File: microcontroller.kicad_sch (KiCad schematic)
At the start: 0 parts

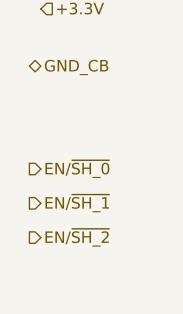
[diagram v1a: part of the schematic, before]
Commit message: Removed hierarchical labels on the sensor board (4 slot) in favour of local labels and connectors. The idea was that the sensor boards are plug-ins so having them defined as separate boards makes more sense. Eventually I think we'll pull them out of the main schematic and design each one separately with the common connector pinout.
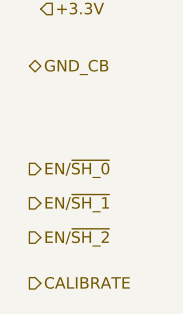
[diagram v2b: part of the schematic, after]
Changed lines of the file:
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@@
+		)
+	)
+	(hierarchical_label "CALIBRATE"
+		(shape output)
+		(at 241.3 142.24 0)
+		(effects
+			(font
+				(size 1.27 1.27)
+			)
+			(justify left)
 		)
 	)

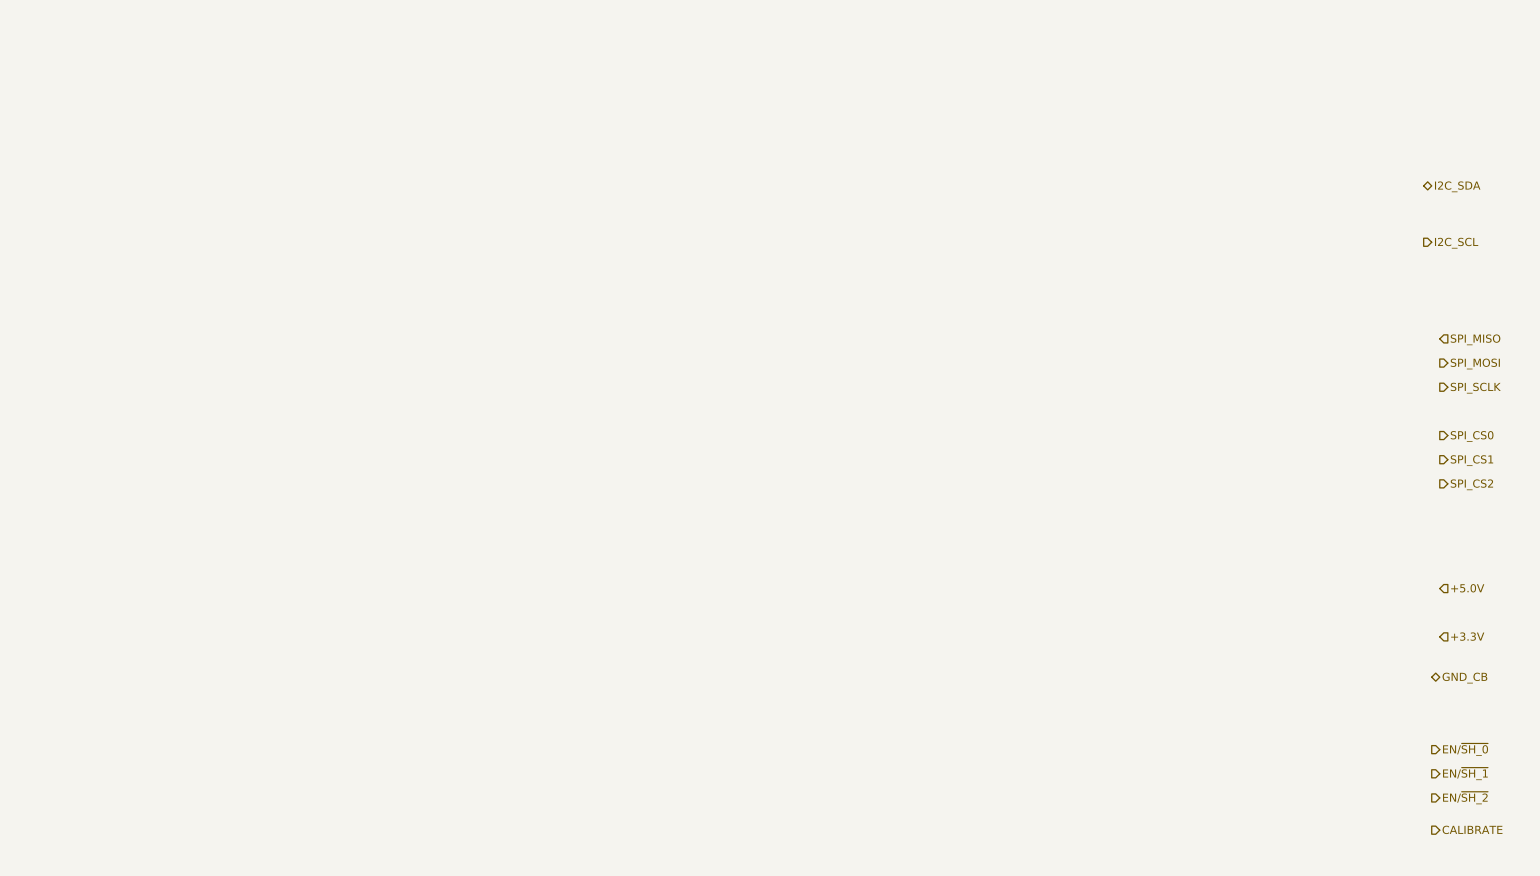
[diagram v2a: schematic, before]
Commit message: Added some notes to otherwise blank pages. Added the full 8 sensor buffers to the 8 sensor analog board. Added a decoupling sub page to same. Changed a couple of sensor labels on base and 4 board just as placeholders
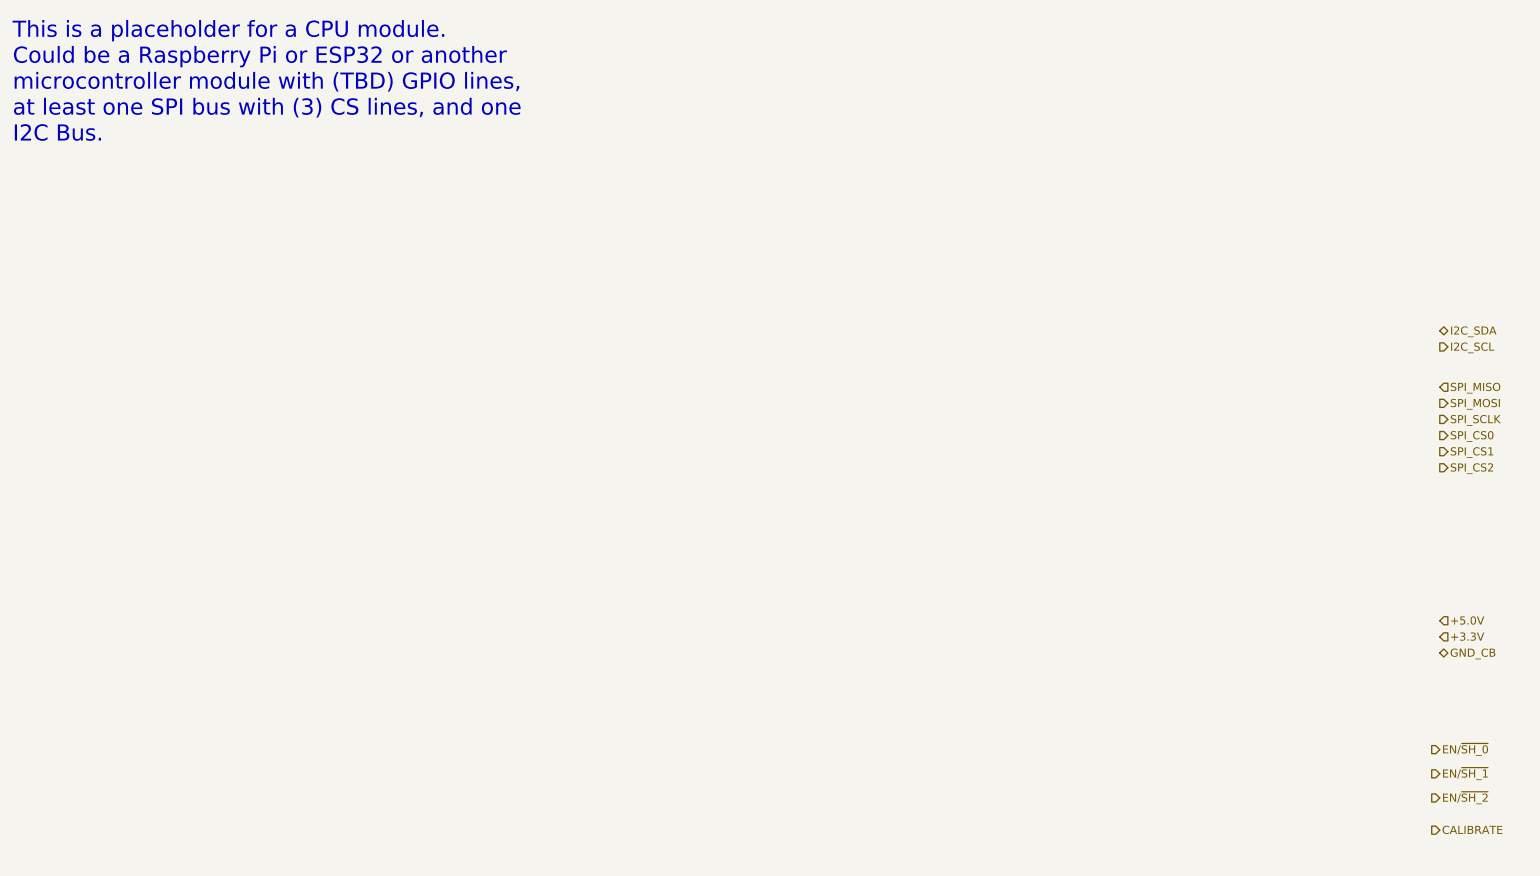
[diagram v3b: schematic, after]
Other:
- note added: "This is a placeholder for a CPU module. Could be a Raspberry Pi or ESP32 or another microcontroller module with (TBD) GPIO lines, at least one SPI bus with (3) CS lines, and one I2C Bus."
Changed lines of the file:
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@@
 	(generator_version "8.0")
 	(paper "A4")
+	(text "This is a placeholder for a CPU module. \nCould be a Raspberry Pi or ESP32 or another\nmicrocontroller module with (TBD) GPIO lines,\nat least one SPI bus with (3) CS lines, and one\nI2C Bus.\n"
+		(exclude_from_sim no)
+		(at 17.526 24.384 0)
+		(effects
+			(font
+				(size 2.54 2.54)
+			)
+			(justify left)
+		)
+	)
 	(hierarchical_label "SPI_MISO"
 		(shape input)
-		(at 242.57 64.77 0)
+		(at 242.57 72.39 0)
 		(effects
 			(font
@@
 	(hierarchical_label "SPI_MOSI"
 		(shape output)
-		(at 242.57 68.58 0)
+		(at 242.57 74.93 0)
 		(effects
 			(font
@@
 	(hierarchical_label "SPI_CS2"
 		(shape output)
-		(at 242.57 87.63 0)
+		(at 242.57 85.09 0)
 		(effects
 			(font
@@
 	(hierarchical_label "I2C_SDA"
 		(shape bidirectional)
-		(at 240.03 40.64 0)
+		(at 242.57 63.5 0)
 		(effects
 			(font
@@
 	(hierarchical_label "SPI_SCLK"
 		(shape output)
-		(at 242.57 72.39 0)
+		(at 242.57 77.47 0)
 		(effects
 			(font
@@
 	(hierarchical_label "+5.0V"
 		(shape input)
-		(at 242.57 104.14 0)
+		(at 242.57 109.22 0)
 		(effects
 			(font
@@
 	(hierarchical_label "SPI_CS1"
 		(shape output)
-		(at 242.57 83.82 0)
+		(at 242.57 82.55 0)
 		(effects
 			(font
@@
 	(hierarchical_label "GND_CB"
 		(shape bidirectional)
-		(at 241.3 118.11 0)
+		(at 242.57 114.3 0)
 		(effects
 			(font
@@
 	(hierarchical_label "I2C_SCL"
 		(shape output)
-		(at 240.03 49.53 0)
+		(at 242.57 66.04 0)
 		(effects
 			(font

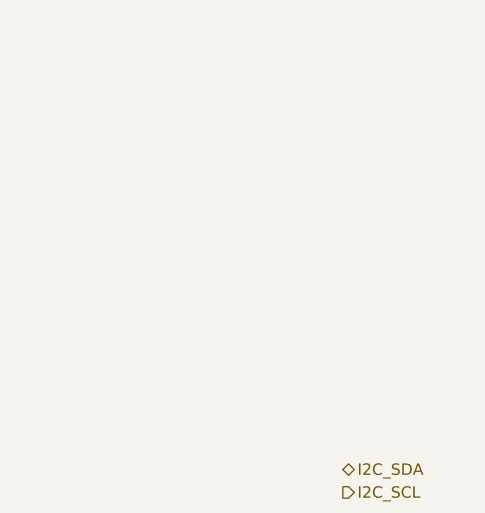
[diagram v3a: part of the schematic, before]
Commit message: Updated the ORP and pH probes with a more appropriate amp. Added some notes. Added a tentative PL-100 adapter circuit. Added Vref buffering. Started move towards ESP32 ADC converter for base sensors.
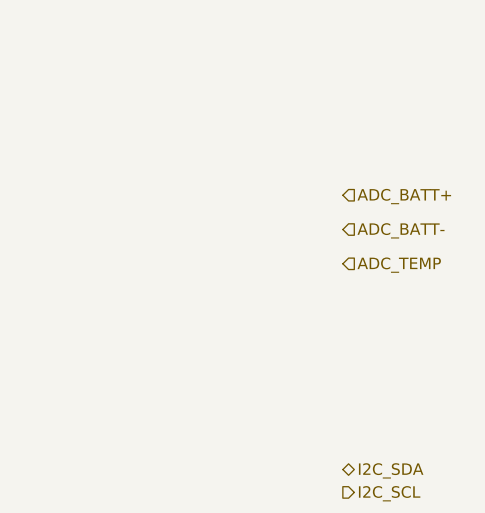
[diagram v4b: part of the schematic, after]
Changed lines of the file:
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@@
+		)
+	)
+	(hierarchical_label "ADC_BATT+"
+		(shape input)
+		(at 242.57 33.02 0)
+		(effects
+			(font
+				(size 1.27 1.27)
+			)
+			(justify left)
 		)
 	)
@@
 		)
 	)
+	(hierarchical_label "ADC_BATT-"
+		(shape input)
+		(at 242.57 36.83 0)
+		(effects
+			(font
+				(size 1.27 1.27)
+			)
+			(justify left)
+		)
+	)
 	(hierarchical_label "SPI_CS0"
 		(shape output)
@@
 		(effects
 			(font
+				(size 1.27 1.27)
+			)
+			(justify left)
+		)
+	)
+	(hierarchical_label "ADC_TEMP"
+		(shape input)
+		(at 242.57 40.64 0)
+		(effects
+			(font

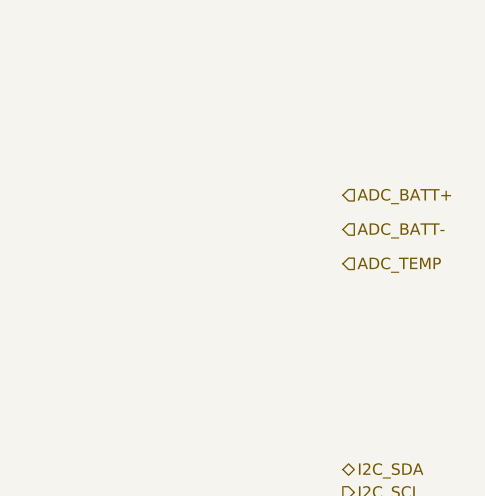
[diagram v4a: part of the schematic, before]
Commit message: Cleaned up a bit Added a SPDT to calibrate signal on the base board Added PTC and MOV to power section
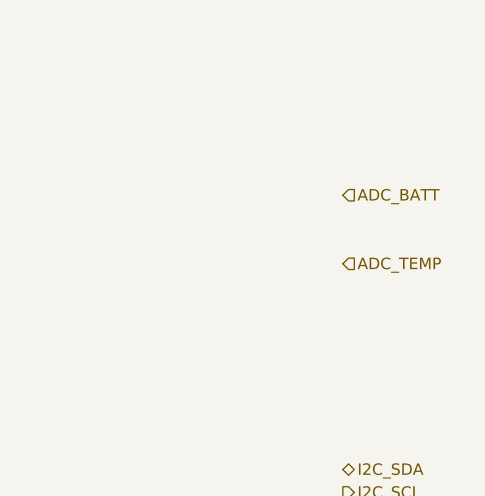
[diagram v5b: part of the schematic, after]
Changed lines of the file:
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@@
 		)
 	)
-	(hierarchical_label "ADC_BATT+"
+	(hierarchical_label "ADC_BATT"
 		(shape input)
 		(at 242.57 33.02 0)
@@
 		(effects
 			(font
-				(size 1.27 1.27)
-			)
-			(justify left)
-		)
-	)
-	(hierarchical_label "ADC_BATT-"
-		(shape input)
-		(at 242.57 36.83 0)
-		(effects
-			(font

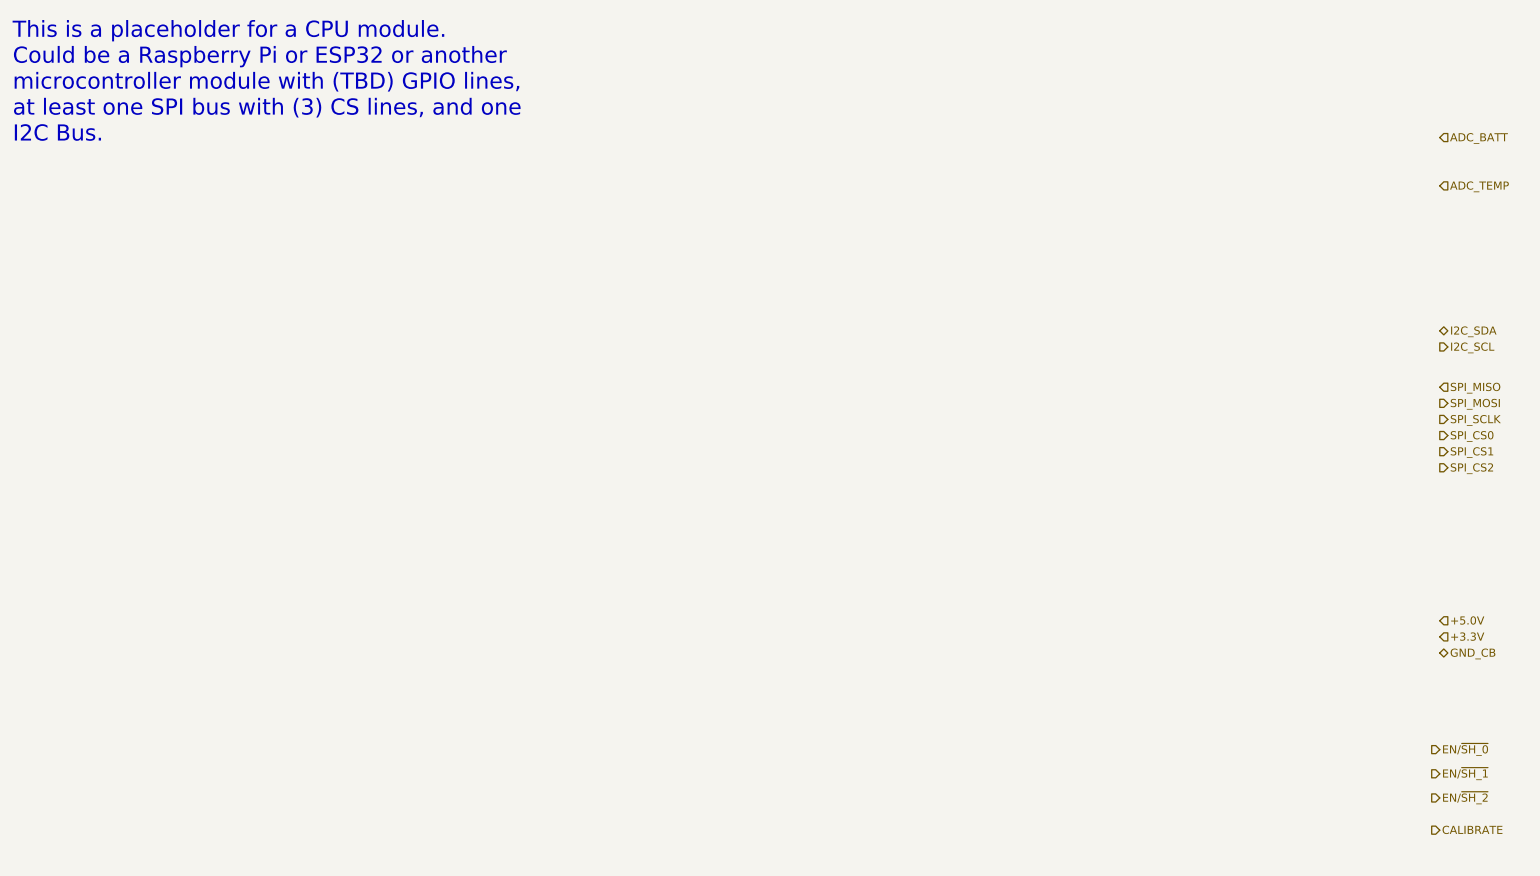
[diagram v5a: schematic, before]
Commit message: Began assigning footprints Cleaned up some of the signalling and added the full prototype sensor suite Added a header for the Atlas Scientific carrier board Added some test points and jumpers Cleaned up the power section Started work on the CPU signal assignment and header sockets
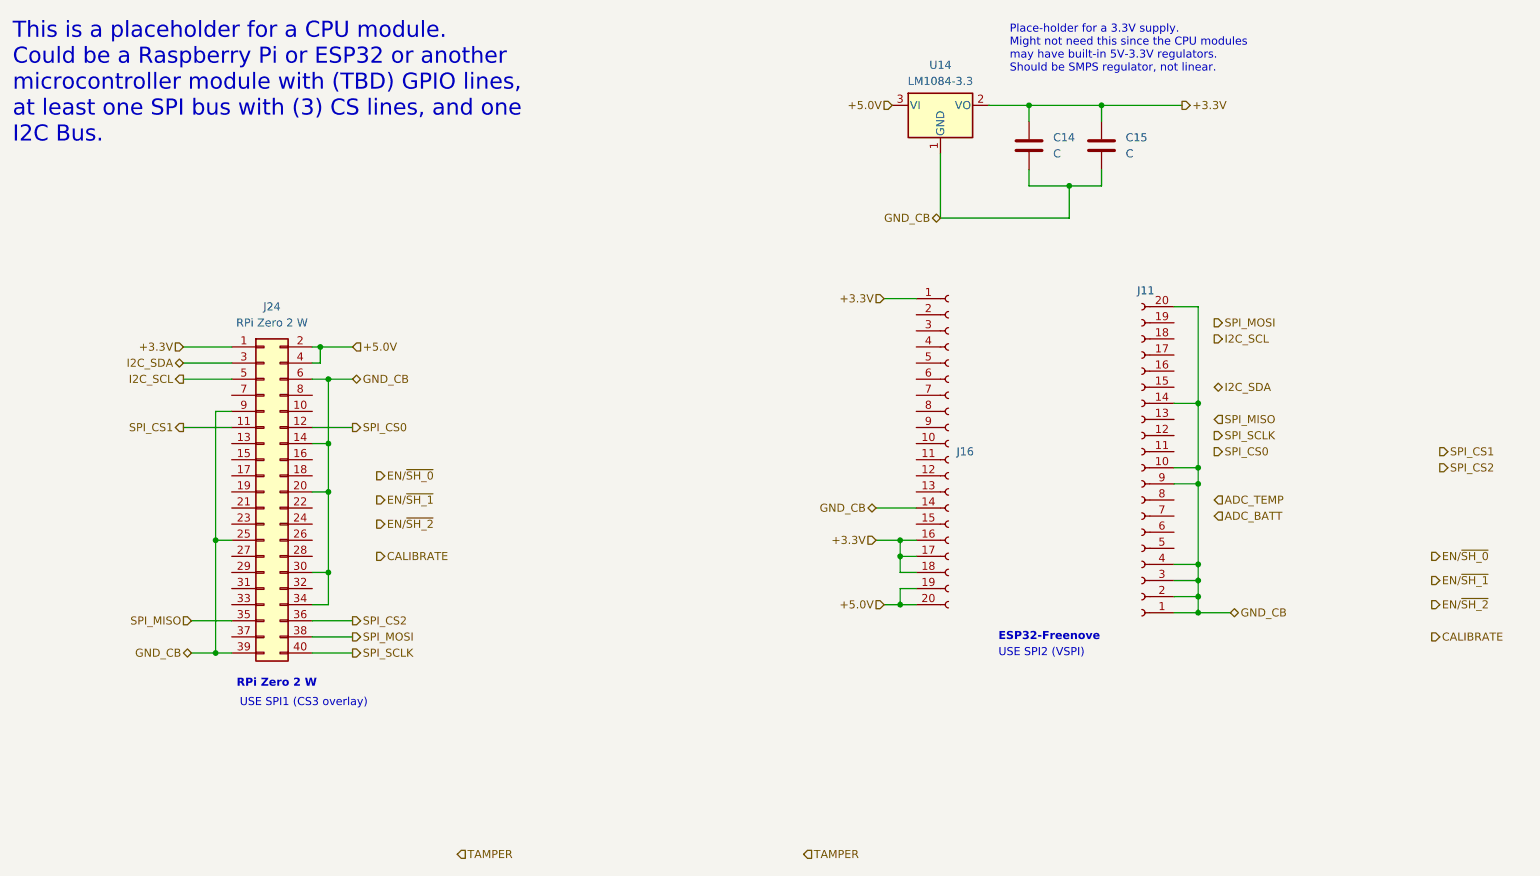
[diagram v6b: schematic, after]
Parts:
- added C14, C15: C, symbol Device:C
- added J11, J16: Conn_01x20_Socket, Connector_PinHeader_1.27mm:PinHeader_1x20_P1.27mm_Vertical_SMD_Pin1Left, symbol Connector:Conn_01x20_Socket
- added J24: RPi Zero 2 W, symbol Connector_Generic:Conn_02x20_Odd_Even
- added U14: LM1084-3.3, symbol Regulator_Linear:LM1084-3.3
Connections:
- net +3.3V: now also C14.1, C15.1, J16.1 (Pin_1), J16.16 (Pin_16), J16.17 (Pin_17), J16.18 (Pin_18), J24.1 (Pin_1), U14.2 (VO)
- net +5.0V: now also J16.19 (Pin_19), J16.20 (Pin_20), J24.2 (Pin_2), J24.4 (Pin_4), U14.3 (VI)
- net GND_CB: now also C14.2, C15.2, J11.1 (Pin_1), J11.10 (Pin_10), J11.14 (Pin_14), J11.2 (Pin_2), J11.20 (Pin_20), J11.3 (Pin_3), J11.4 (Pin_4), J11.9 (Pin_9), J16.14 (Pin_14), J24.14 (Pin_14), J24.20 (Pin_20), J24.25 (Pin_25), J24.30 (Pin_30), J24.34 (Pin_34), J24.39 (Pin_39), J24.6 (Pin_6), J24.9 (Pin_9), U14.1 (GND)
- net I2C_SCL: now also J24.5 (Pin_5)
- net I2C_SDA: now also J24.3 (Pin_3)
- net SPI_CS0: now also J24.12 (Pin_12)
- net SPI_CS1: now also J24.11 (Pin_11)
- net SPI_CS2: now also J24.36 (Pin_36)
- net SPI_MISO: now also J24.35 (Pin_35)
- net SPI_MOSI: now also J24.38 (Pin_38)
- net SPI_SCLK: now also J24.40 (Pin_40)
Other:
- note added: "ESP32-Freenove"
- note added: "Place-holder for a 3.3V supply. Might not need this since the CPU modules may have built-in 5V-3.3V regulators. Should be SMPS regulator, not linear."
- note added: "RPi Zero 2 W"
- note added: "USE SPI1 (CS3 overlay)"
- note added: "USE SPI2 (VSPI)"
